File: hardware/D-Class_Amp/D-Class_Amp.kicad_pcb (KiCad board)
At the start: 2 copper layers, 52 parts, among them Q301 PHP23NQ11T, U201 LM324, U301 NCP1117-12_TO252, U302 IR21834, U303 IR21834, U501 MAX4016, U502 LM2903

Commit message: Started input stage layout
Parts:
- added R201: 100k, Resistor_SMD:R_0805_2012Metric_Pad1.20x1.40mm_HandSolder, F.Cu at (56.9, 138.7)
- added R206: 100k, Resistor_SMD:R_0805_2012Metric_Pad1.20x1.40mm_HandSolder, F.Cu at (52.8, 142.2)
- TP108: value TestPoint -> ~Speaker_Out
- moved TP201 48.4 mm to (56.4, 134.1)
- moved R203 47.8 mm to (60.9, 138.7)
- moved R202 47.0 mm to (56.9, 142.2)
- moved C204 43.2 mm to (60.9, 142.2)
- moved C203 36.4 mm to (52.8, 138.7)
- moved R209 35.7 mm to (65.5, 150.4)
- moved TP202 34.8 mm to (75.7, 153.9)
- moved C206 31.3 mm to (88.9, 117.3)
- moved RV201 30.6 mm to (70.1, 157.5)
- moved C201 24.0 mm to (65.0, 138.7)
- moved R210 20.8 mm to (95.5, 148.8)
- moved C205 19.7 mm to (99.5, 131.6)
- moved U201 17.8 mm to (88.9, 124.2)
- moved R204 17.7 mm to (99.6, 135.1)
- moved C202 17.4 mm to (104.1, 131.6)
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
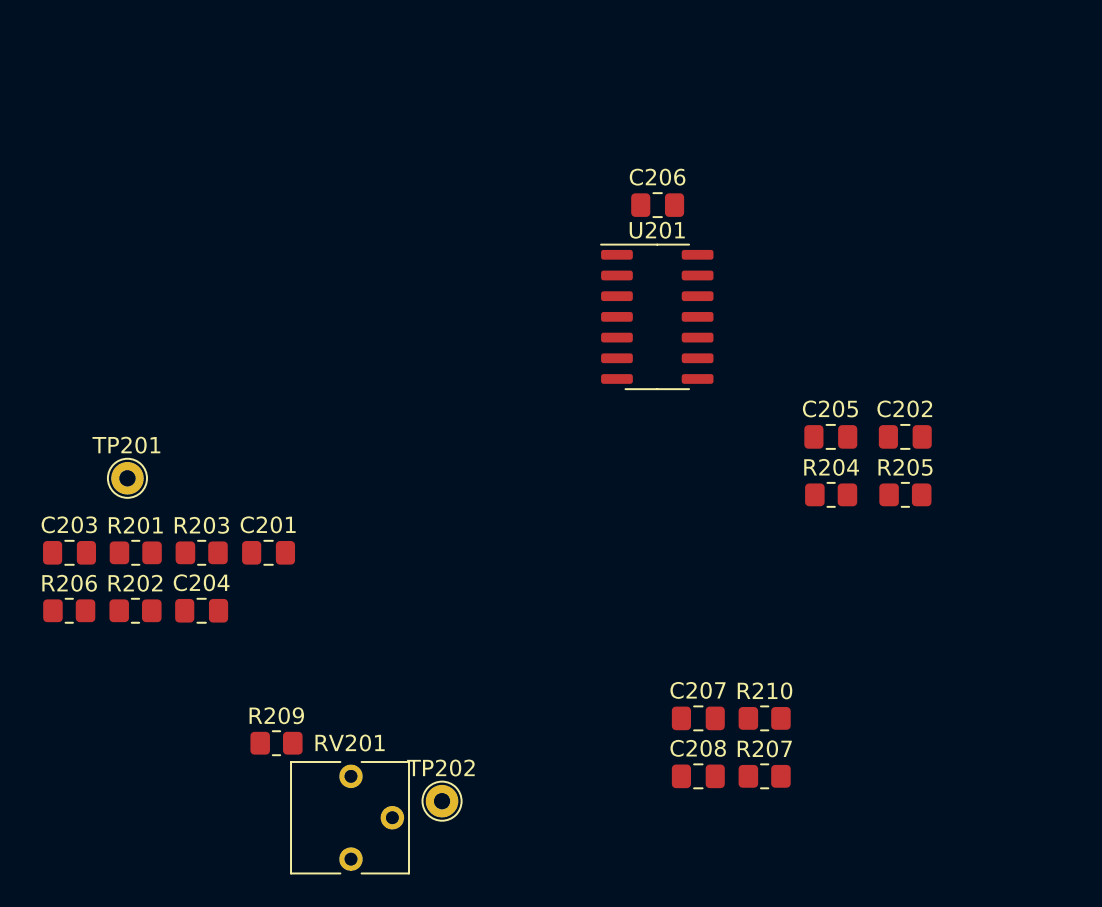
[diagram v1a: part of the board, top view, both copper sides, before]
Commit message: Positioned passives around LM324
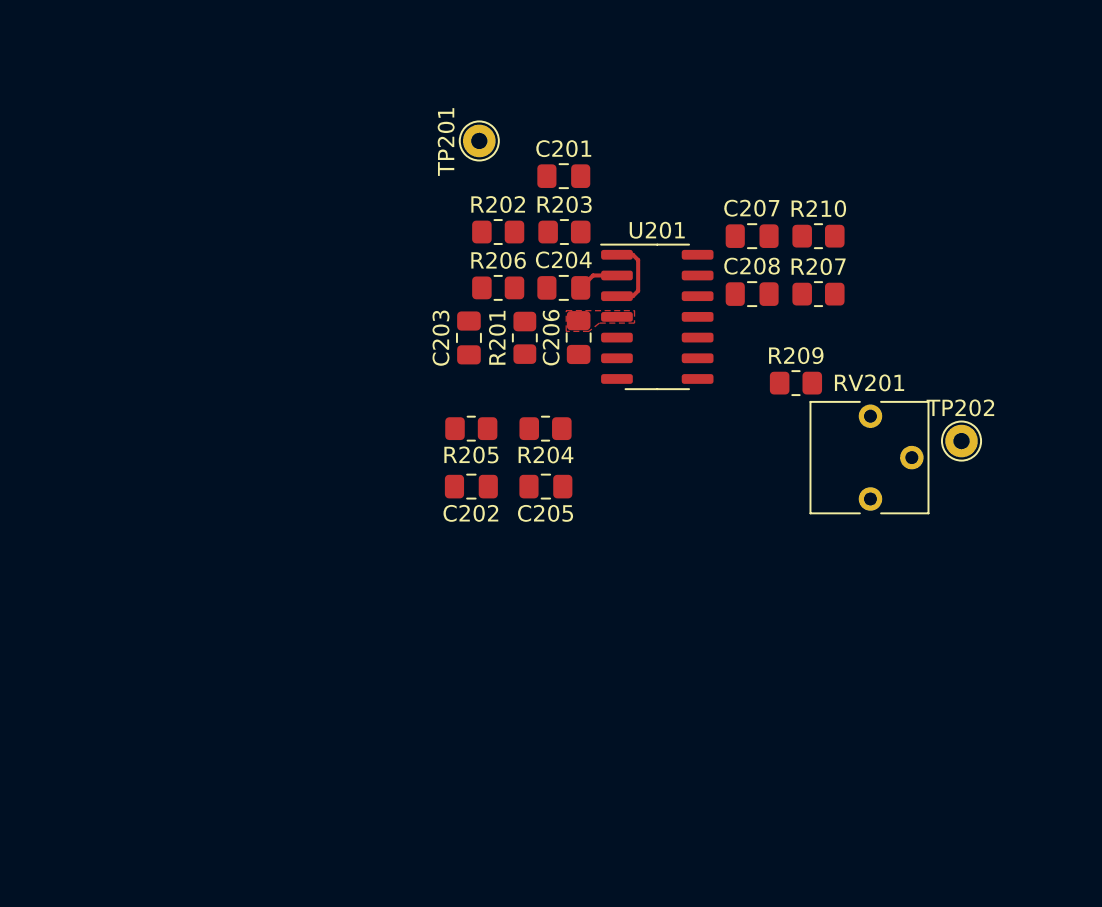
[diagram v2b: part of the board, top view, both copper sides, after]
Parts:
- moved TP202 38.8 mm to (107.6, 131.8)
- moved R209 38.8 mm to (97.4, 128.3)
- moved RV201 38.8 mm to (102.0, 135.4)
- moved R206 32.9 mm to (79.1, 122.4)
- moved R202 32.2 mm to (79.1, 119.0), turned to 180 degrees
- moved TP201 29.9 mm to (78.0, 113.4), turned to 90 degrees
- moved C208 29.8 mm to (94.7, 122.8)
- moved R207 29.8 mm to (98.8, 122.8)
- moved C207 29.8 mm to (94.7, 119.3)
- moved R210 29.8 mm to (98.8, 119.3)
- moved C204 29.8 mm to (83.2, 122.4)
- moved R203 29.7 mm to (83.2, 119.0)
- moved C201 29.4 mm to (83.2, 115.6), turned to 180 degrees
- moved C203 27.8 mm to (77.3, 125.5), turned to 90 degrees
- moved R201 27.3 mm to (80.8, 125.5), turned to 90 degrees
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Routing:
- net /Input_Stage/A_OUT: track 0.00 -> 4.76 mm
- net Net-(C204-Pad2): track 0.00 -> 2.54 mm
- added copper zone on F.Cu, net +5V

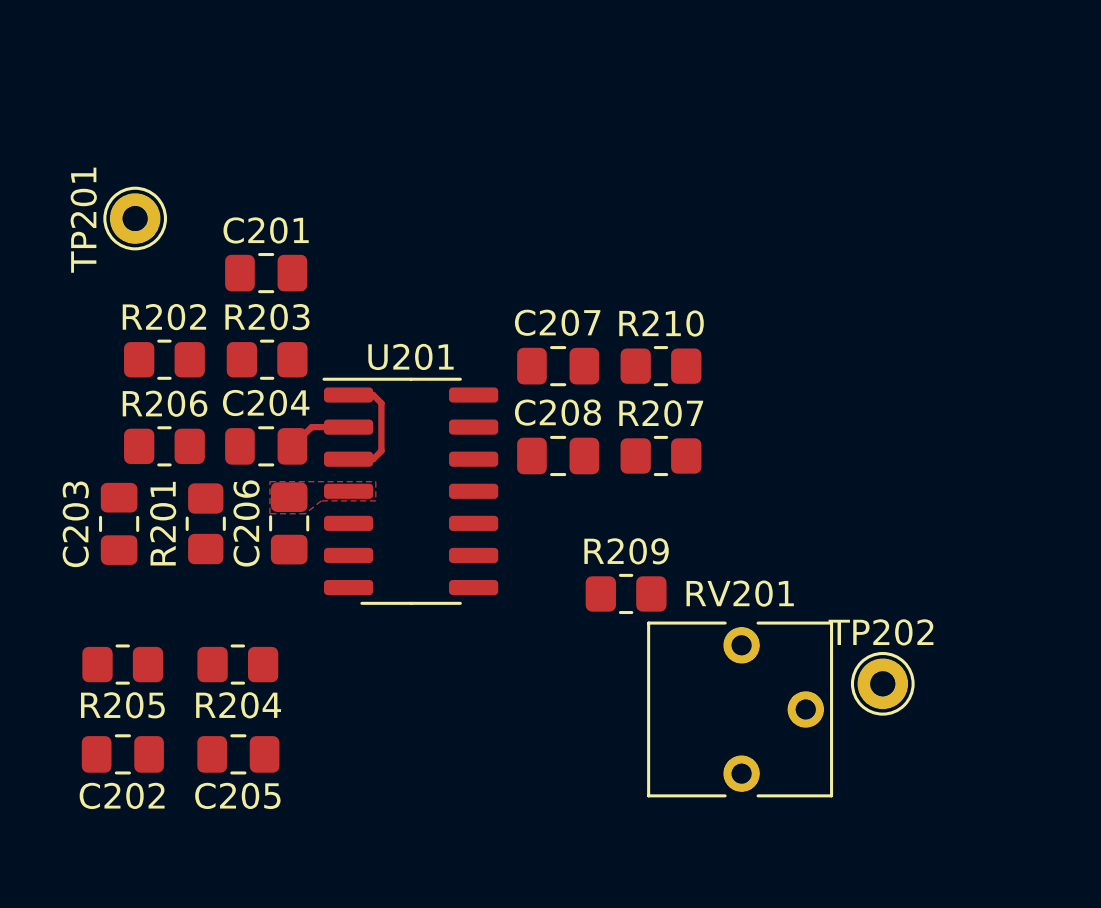
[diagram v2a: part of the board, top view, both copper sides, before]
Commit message: Positioned all passives for the input stage; started trace layout
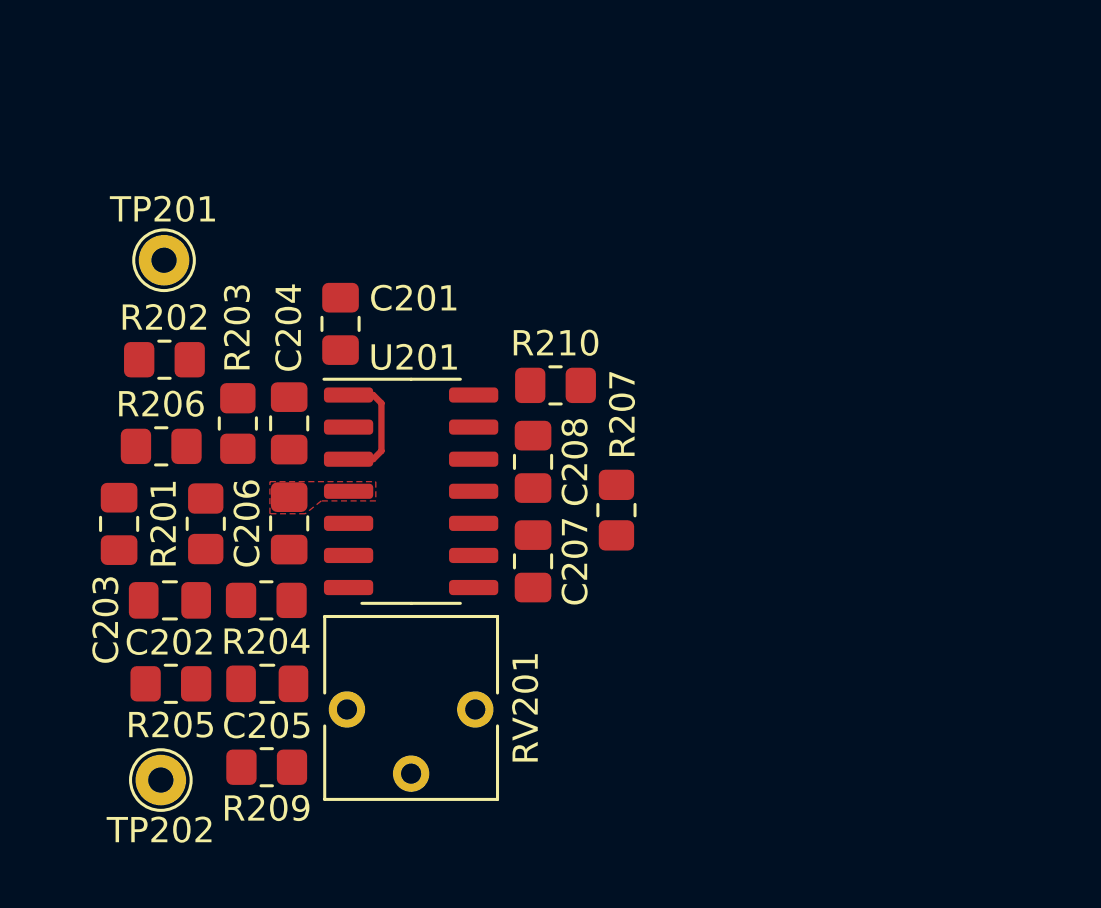
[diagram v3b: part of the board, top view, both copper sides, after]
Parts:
- moved TP202 28.8 mm to (79.0, 135.6), turned to 180 degrees
- moved RV201 15.8 mm to (86.4, 132.8), turned to 270 degrees
- moved R209 15.8 mm to (83.2, 135.1), turned to 180 degrees
- moved C207 7.79 mm to (93.7, 127.0), turned to 270 degrees
- moved C202 6.37 mm to (79.4, 128.5)
- moved R210 4.24 mm to (94.6, 120.0), turned to 180 degrees
- moved C201 3.56 mm to (86.1, 117.6), turned to 90 degrees
- moved C205 3.02 mm to (83.2, 131.8)
- moved R204 2.78 mm to (83.2, 128.5)
- moved R203 2.78 mm to (82.0, 121.5), turned to 90 degrees
- moved R207 2.77 mm to (97.0, 125.0), turned to 270 degrees
- moved R205 2.05 mm to (79.4, 131.8)
- moved TP201 2.01 mm to (79.1, 115.1), turned to 0 degrees
- moved C204 1.29 mm to (84.1, 121.5), turned to 270 degrees
- moved C208 1.02 mm to (93.7, 123.0), turned to 270 degrees
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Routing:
- net Net-(C204-Pad2): track 2.54 -> 0.00 mm

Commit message: layed out the phase phucker
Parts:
- removed the C301 at (108.2, 91.7)
- removed the C302 at (108.2, 94.7)
- removed R206: 100k, Resistor_SMD:R_0805_2012Metric_Pad1.20x1.40mm_HandSolder
- removed the U301 at (120.0, 81.2)
- added C101: 10u 16V, Capacitor_SMD:C_0805_2012Metric_Pad1.18x1.45mm_HandSolder, F.Cu at (172.7, 178.4)
- added C102: 10u 16V, Capacitor_SMD:C_0805_2012Metric_Pad1.18x1.45mm_HandSolder, F.Cu at (178.4, 170.4)
- added C103: 1u 16V, Capacitor_SMD:C_0805_2012Metric_Pad1.18x1.45mm_HandSolder, F.Cu at (178.4, 173.4)
- added C104: 1u 16V, Capacitor_SMD:C_0805_2012Metric_Pad1.18x1.45mm_HandSolder, F.Cu at (183.2, 170.4)
- added C401: 3.3u 50V, Capacitor_SMD:CP_Elec_4x5.4, F.Cu at (201.1, 149.9)
- added C402: 3.3u 50V, Capacitor_SMD:CP_Elec_4x5.4, F.Cu at (212.0, 142.0)
- added C403: 16u 500V, C4AQLLW5160A33K:C4AQLLW5160A33K_film_capacitor, F.Cu at (186.0, 133.7)
- added C501: 10u 16V, Capacitor_SMD:C_0805_2012Metric_Pad1.18x1.45mm_HandSolder, F.Cu at (250.1, 134.9)
- added C502: 10u 16V, Capacitor_SMD:C_0805_2012Metric_Pad1.18x1.45mm_HandSolder, F.Cu at (254.9, 134.9)
- added JP1: HPF_BYPASS, Jumper:SolderJumper-2_P1.3mm_Open_TrianglePad1.0x1.5mm, F.Cu at (97.3, 127.0)
- added L1: 270u, Inductor_THT:L_Toroid_Vertical_L31.8mm_W15.9mm_P13.50mm_Bourns_5700, F.Cu at (224.8, 123.0)
- added L401: 270u, Inductor_THT:L_Toroid_Vertical_L31.8mm_W15.9mm_P13.50mm_Bourns_5700, F.Cu at (180.5, 149.5)
- added Q502: PHP23NQ11T, Package_TO_SOT_THT:TO-251-3-1EP_Horizontal_TabDown, F.Cu at (249.5, 131.7)
- added Q503: PHP23NQ11T, Package_TO_SOT_THT:TO-251-3-1EP_Horizontal_TabDown, F.Cu at (257.6, 131.7)
- added Q504: PHP23NQ11T, Package_TO_SOT_THT:TO-251-3-1EP_Horizontal_TabDown, F.Cu at (265.7, 131.7)
- added R301: 10K, Resistor_SMD:R_0805_2012Metric_Pad1.20x1.40mm_HandSolder, F.Cu at (254.8, 141.6)
- added R302: 10K, Resistor_SMD:R_0805_2012Metric_Pad1.20x1.40mm_HandSolder, F.Cu at (250.1, 141.6)
- added TP109: Power GND, TestPoint:TestPoint_THTPad_D2.0mm_Drill1.0mm, F.Cu at (182.8, 173.9)
- added TP110: Signal GND, TestPoint:TestPoint_THTPad_D2.0mm_Drill1.0mm, F.Cu at (177.2, 179.0)
- added TP501: HO, TestPoint:TestPoint_THTPad_D2.0mm_Drill1.0mm, F.Cu at (274.1, 134.6)
- added TP502: LO, TestPoint:TestPoint_THTPad_D2.0mm_Drill1.0mm, F.Cu at (274.1, 130.5)
- added TP503: ~HO, TestPoint:TestPoint_THTPad_D2.0mm_Drill1.0mm, F.Cu at (274.1, 126.5)
- added TP504: ~LO, TestPoint:TestPoint_THTPad_D2.0mm_Drill1.0mm, F.Cu at (274.1, 122.4)
- added U101: NCP1117-12_TO252, Package_TO_SOT_SMD:TO-252-2, F.Cu at (169.9, 172.9)
- added U102: MCP1799T-5002H_TT, Package_TO_SOT_SMD:SOT-23_Handsoldering, F.Cu at (167.1, 179.2)
- C201: value 100n -> 120n
- C202: value 100n -> 750n
- C207: value 100n -> 2.2u
- C208: value 100n -> 1.2u
- C301: renamed from C501; value 100n -> 100n 16V
- C303: renamed from C503; value 100n -> 100n 16V
- C503: renamed from C303; value .47u -> 0.47u 50V
- C504: renamed from C304; value 0.47u -> 0.47u 50V
- R202: value 5.6k -> 4.3k
- R203: value 8.2k -> 5.6k
- R204: value 5.6k -> 1.5k
- R205: value 8.2k -> 2.4k
- R210: value 8.2k -> 15k
- RV201: value 50k -> 20k
- U301: renamed from U501; value MAX4016 -> TL972
- U302: renamed from U502; value LM2903 -> LMV393; footprint Package_SO:SOIC-8_3.9x4.9mm_P1.27mm -> Package_SO:VSSOP-8_3.0x3.0mm_P0.65mm
- moved TP202 15.4 mm to (94.4, 134.6), turned to 270 degrees
- moved R209 11.4 mm to (93.7, 130.8), turned to 270 degrees
- moved R204 4.45 mm to (83.3, 133.0)
- moved C202 4.45 mm to (79.5, 133.0)
- moved TP201 3.07 mm to (79.5, 118.1), turned to 90 degrees
- moved R202 2.74 mm to (79.8, 121.7), turned to 270 degrees
- moved C203 2.41 mm to (79.8, 125.5)
- moved C205 2.16 mm to (83.2, 129.7)
- moved R205 2.16 mm to (79.4, 129.7)
- moved R207 2.02 mm to (97.0, 122.9)
- moved C201 1.27 mm to (86.8, 118.6), turned to 180 degrees
- moved R201 1.02 mm to (81.8, 125.5)
- moved R203 0.29 mm to (81.8, 121.7)
- moved C204 0.15 mm to (84.1, 121.7)
- moved RV201 0.13 mm to (86.4, 132.7)
- renumbered C502 to C302, Q301 to Q501, R501 to R303, R504 to R304, R505 to R305, R506 to R306, R301 to R501, R302 to R502, R303 to R503, R304 to R504, R305 to R505, R306 to R506, U302 to U502, U303 to U503
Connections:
- R201 pad 1: +5V -> +2V5
- U201 pad 10: Net-(RV201-Pad2) -> /Input_Stage/B_OUT
- U201 pad 12: /Input_Stage/FILT_OUT -> Net-(C208-Pad1)
- U201 pad 13: Net-(C208-Pad1) -> /Input_Stage/FILT_OUT
- U201 pad 2: Net-(C204-Pad2) -> /Input_Stage/A_OUT
- U201 pad 3: /Input_Stage/A_OUT -> Net-(C204-Pad2)
- U201 pad 5: /Input_Stage/B_OUT -> Net-(C205-Pad2)
- U201 pad 6: Net-(C205-Pad2) -> /Input_Stage/B_OUT
- U201 pad 9: /Input_Stage/B_OUT -> Net-(RV201-Pad2)
- U301 pad 2: +2V5 -> /S-PWM_Gen/V_ref
- U301 pad 5: +2V5 -> /S-PWM_Gen/V_ref
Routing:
- net /Input_Stage/A_OUT: track 4.76 -> 21.7 mm, vias 0 -> 2
- net /Input_Stage/B_OUT: track 0.00 -> 17.0 mm, vias 0 -> 3
- net Net-(RV201-Pad2): track 0.00 -> 15.5 mm
- net /Input_Stage/FILT_OUT: track 0.00 -> 15.2 mm
- net +2V5: track 0.00 -> 13.1 mm, vias 0 -> 4
- net Net-(C205-Pad2): track 0.00 -> 12.6 mm
- net /Input_Stage/C_OUT: track 0.00 -> 12.0 mm
- net Net-(C203-Pad1): track 0.00 -> 11.0 mm
- net Net-(C202-Pad2): track 0.00 -> 10.1 mm
- net Net-(C201-Pad2): track 0.00 -> 6.90 mm
- net Net-(C207-Pad1): track 0.00 -> 5.22 mm
- net Net-(C208-Pad1): track 0.00 -> 4.77 mm
- net Net-(C204-Pad2): track 0.00 -> 4.75 mm
- added copper zone on F.Cu, net GNDS
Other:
- board text added: "THE PHASE PHUCKER 6000X"

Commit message: Updated input filter layout
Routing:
- net +5V: track 0.00 -> 9.52 mm
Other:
- board text removed: "THE PHASE PHUCKER 6000X"

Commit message: updated the BOM
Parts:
- added C104: 1000u 50V, Capacitor_THT:CP_Radial_D10.0mm_P5.00mm, F.Cu at (222.6, 176.7)
- added C202: 100u 6.3V, Capacitor_SMD:CP_Elec_4x5.4, F.Cu at (249.0, 173.9)
- added C401: 1u 50V, Capacitor_SMD:CP_Elec_4x5.4, F.Cu at (228.7, 135.5)
- added C402: 1u 50V, Capacitor_SMD:CP_Elec_4x5.4, F.Cu at (236.4, 135.5)
- added D501: UG1B-E3/54r, Diode_THT:D_DO-41_SOD81_P7.62mm_Horizontal, F.Cu at (274.4, 134.7)
- added D502: UG1B-E3/54r, Diode_THT:D_DO-41_SOD81_P7.62mm_Horizontal, F.Cu at (274.4, 139.0)
- added J102: AudioJack2, Connector_Audio:Jack_3.5mm_CUI_SJ-3523-SMT_Horizontal, F.Cu at (212.9, 180.5)
- added JP201: Filter_bypass, Jumper:SolderJumper-3_P1.3mm_Bridged12_RoundedPad1.0x1.5mm_NumberLabels, F.Cu at (255.7, 172.7)
- added L402: 150u, IND_HCTI-150-5.0:IND_HCTI-150-5.0, F.Cu at (215.8, 149.6)
- added R101: 10k, Resistor_SMD:R_0805_2012Metric_Pad1.20x1.40mm_HandSolder, F.Cu at (221.4, 184.0)
- added R102: 10k, Resistor_SMD:R_0805_2012Metric_Pad1.20x1.40mm_HandSolder, F.Cu at (233.2, 172.4)
- added TP301: Square, TestPoint:TestPoint_THTPad_D2.0mm_Drill1.0mm, F.Cu at (274.6, 146.6)
- added TP302: Triangle, TestPoint:TestPoint_THTPad_D2.0mm_Drill1.0mm, F.Cu at (278.6, 146.6)
- C201: renamed from C206; value 100n -> 100n 16V
- C203: renamed from C201; value 120n -> 150n 16V
- C204: value 100n -> 100n 16V
- C205: renamed from C207; value 2.2u -> 2.2u 16V
- C206: renamed from C202; value 750n -> 680n 16V
- C207: renamed from C208; value 1.2u -> 1.2u 16V
- C208: renamed from C205; value 100n -> 100n 16V
- C403: value 16u 500V -> 10u 700V
- L401: value 270u -> 150u
- R201: value 100k -> 10k
- R301: renamed from R303; value 10K -> 10k
- R302: renamed from R304; value 6.8k -> 1k
- moved C208 56.0 mm to (35.7, 99.9)
- moved R206 56.0 mm to (31.9, 99.9)
- moved R207 56.0 mm to (49.5, 93.2)
- moved TP202 56.0 mm to (46.9, 104.9)
- moved U201 56.0 mm to (41.4, 94.5)
- moved C201 56.0 mm to (36.6, 95.8)
- moved C203 56.0 mm to (32.3, 95.8)
- moved C203 56.0 mm to (39.3, 88.9)
- moved C204 56.0 mm to (36.6, 91.9)
- moved C205 56.0 mm to (46.2, 97.3)
- moved C206 56.0 mm to (32.0, 103.3)
- moved C207 56.0 mm to (46.2, 93.3)
- moved JP1 56.0 mm to (49.8, 97.3)
- moved R201 56.0 mm to (34.3, 95.8)
- moved R202 56.0 mm to (32.3, 91.9)
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- renumbered C104 to C105, C503 to C502, C504 to C503, C502 to C504, R209 to R204, R204 to R205, R205 to R206, R210 to R208, R305 to R303, R306 to R304, TP109 to TP101, TP110 to TP102, TP101 to TP103, TP102 to TP104, TP103 to TP105, TP104 to TP106, TP105 to TP107, TP106 to TP108, TP107 to TP109, TP108 to TP110, U502 to U501, U503 to U502
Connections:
- R201 pad 2: Net-(C203-Pad1) -> Net-(C202-Pad1)
- R202 pad 2: Net-(C203-Pad1) -> Net-(C202-Pad1)
- R207 pad 1: /Input_Stage/FILT_OUT -> Net-(JP201-Pad1)
- TP201 pad 1: Net-(C203-Pad1) -> Net-(C202-Pad1)
- U201 pad 13: /Input_Stage/FILT_OUT -> Net-(JP201-Pad1)
- U201 pad 14: /Input_Stage/FILT_OUT -> Net-(JP201-Pad1)
- U301 pad 2: /S-PWM_Gen/V_ref -> +2V5
- U301 pad 5: /S-PWM_Gen/V_ref -> +2V5

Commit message: Designed the triangle generator PCB layout, and the power switching stage layout
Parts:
- removed the C203 at (32.3, 95.8)
- removed the C401 at (201.1, 149.9)
- removed the C402 at (212.0, 142.0)
- removed JP1: HPF_BYPASS, Jumper:SolderJumper-2_P1.3mm_Open_TrianglePad1.0x1.5mm
- removed L1: 270u, Inductor_THT:L_Toroid_Vertical_L31.8mm_W15.9mm_P13.50mm_Bourns_5700
- removed the R301 at (254.8, 141.6)
- removed the R302 at (250.1, 141.6)
- added H101: VDD, MountingHole:MountingHole_3mm_Pad_Via, F.Cu at (103.6, 105.4)
- added H102: GND, MountingHole:MountingHole_3mm_Pad_Via, F.Cu at (96.1, 105.4)
- added NT101: Net-Tie_2, NetTie:NetTie-2_SMD_Pad2.0mm, F.Cu at (55.6, 98.0)
- C301, C303: footprint Resistor_SMD:R_0805_2012Metric_Pad1.20x1.40mm_HandSolder -> Capacitor_SMD:C_0805_2012Metric_Pad1.18x1.45mm_HandSolder
- C403: footprint C4AQLLW5160A33K:C4AQLLW5160A33K_film_capacitor -> C4AQJLU5100M19J:C4AQJLU5100M19J_film_capacitor
- L401: footprint Inductor_THT:L_Toroid_Vertical_L31.8mm_W15.9mm_P13.50mm_Bourns_5700 -> IND_HCTI-150-5.0:IND_HCTI-150-5.0
- Q501, Q502, Q503, Q504: footprint Package_TO_SOT_THT:TO-251-3-1EP_Horizontal_TabDown -> PHP23NQ11T:PHP23NQ11T
- U302: footprint Package_SO:VSSOP-8_3.0x3.0mm_P0.65mm -> Package_SO:SOIC-8_3.9x4.9mm_P1.27mm
- moved TP302 267.6 mm to (45.3, 15.4)
- moved TP301 261.4 mm to (45.5, 20.7)
- moved C202 235.4 mm to (27.1, 95.6), turned to 180 degrees
- moved JP201 221.4 mm to (51.9, 86.2)
- moved J102 217.4 mm to (12.4, 96.4), turned to 180 degrees
- moved TP502 213.5 mm to (71.4, 63.8)
- moved D501 208.1 mm to (77.3, 67.9), turned to 180 degrees
- moved TP501 208.1 mm to (78.5, 63.8)
- moved D502 205.0 mm to (77.3, 82.5), turned to 180 degrees
- moved TP504 204.4 mm to (71.1, 98.3)
- moved TP503 197.4 mm to (78.7, 98.3)
- moved R102 192.0 mm to (61.7, 86.1), turned to 90 degrees
- moved C504 189.8 mm to (70.1, 91.7), turned to 90 degrees
- moved C501 189.1 mm to (70.1, 77.1), turned to 90 degrees
- moved R101 189.0 mm to (59.7, 86.1), turned to 270 degrees
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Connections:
- C103 pad 2: GND -> GNDS
- C105 pad 2: GND -> GNDS
- U102 pad 1: GND -> GNDS
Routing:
- net +12V: track 0.00 -> 37.0 mm, vias 0 -> 2
- net /Power_Stage/~S-PWM: track 0.00 -> 23.2 mm
- net /Power_Stage/S-PWM: track 0.00 -> 22.3 mm
- net Net-(R302-Pad2): track 0.00 -> 19.0 mm
- net /S-PWM_Gen/sig_triangle: track 0.00 -> 18.5 mm
- net Net-(R301-Pad1): track 0.00 -> 14.0 mm
- net Net-(JP201-Pad1): track 0.00 -> 13.8 mm
- net /Input_Stage/C_OUT: track 12.0 -> 24.2 mm
- net GNDS: track 0.00 -> 11.3 mm, vias 0 -> 1
- net Net-(C203-Pad1): track 11.0 -> 0.00 mm
- net Net-(C302-Pad2): track 0.00 -> 11.0 mm
- net Net-(R503-Pad2): track 0.00 -> 8.64 mm
- net Net-(C202-Pad1): track 0.00 -> 8.58 mm
- net Net-(R505-Pad2): track 0.00 -> 8.51 mm
- net Net-(C503-Pad1): track 0.00 -> 8.28 mm
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- added copper zone on B.Cu, net (none)
- added copper zone on F.Cu, net +2V5
- added copper zone on F.Cu, net /Power_Stage/S-PWM
- added copper zone on F.Cu, net /Power_Stage/~S-PWM
- added copper zone on F.Cu, net GND
- added copper zone on B.Cu, net VDD
- added copper zone on F.Cu, net VDD
